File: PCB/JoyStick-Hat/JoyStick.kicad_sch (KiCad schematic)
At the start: 18 parts, among them J10 Conn_01x02_Pin, J11 Conn_01x02_Pin, J12 Conn_01x02_Pin, J13 Conn_01x02_Pin, J14 Conn_01x03_Pin, J15 Conn_01x03_Pin, J8 Conn_01x04_Pin, J9 Conn_01x04_Pin

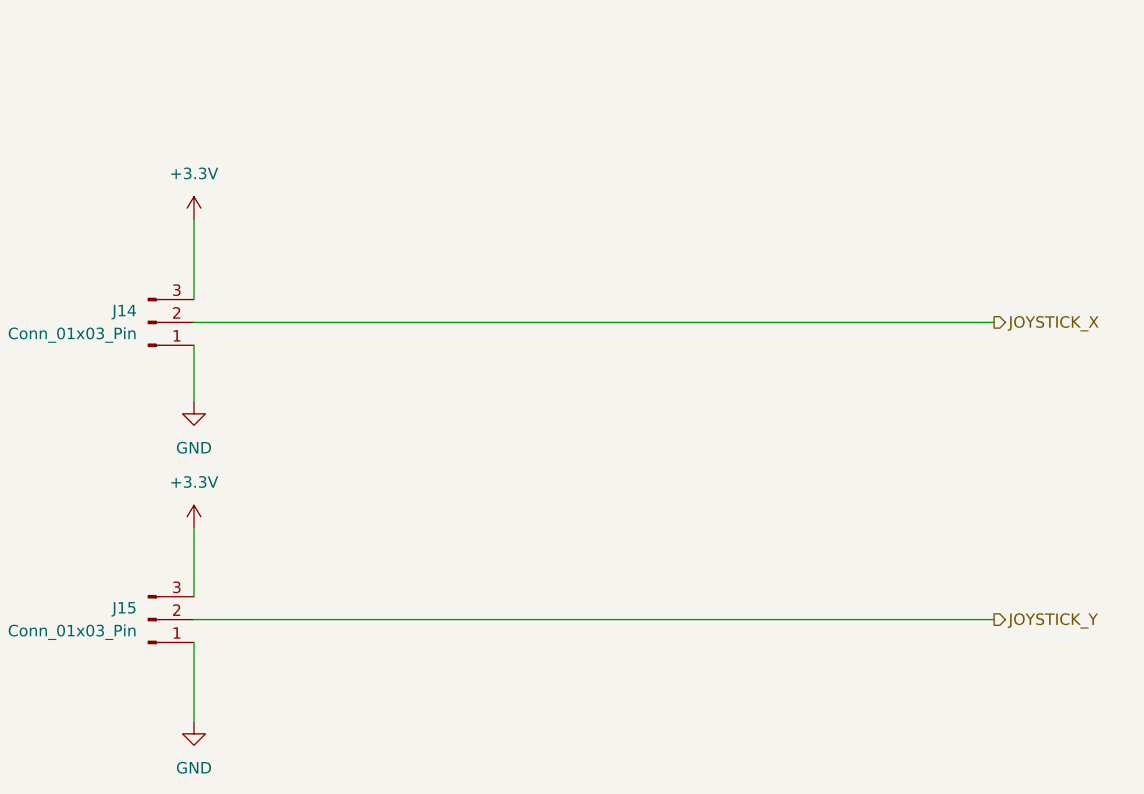
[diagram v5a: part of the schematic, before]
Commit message: Board Shape and Layout
Board Shape added and layout started !
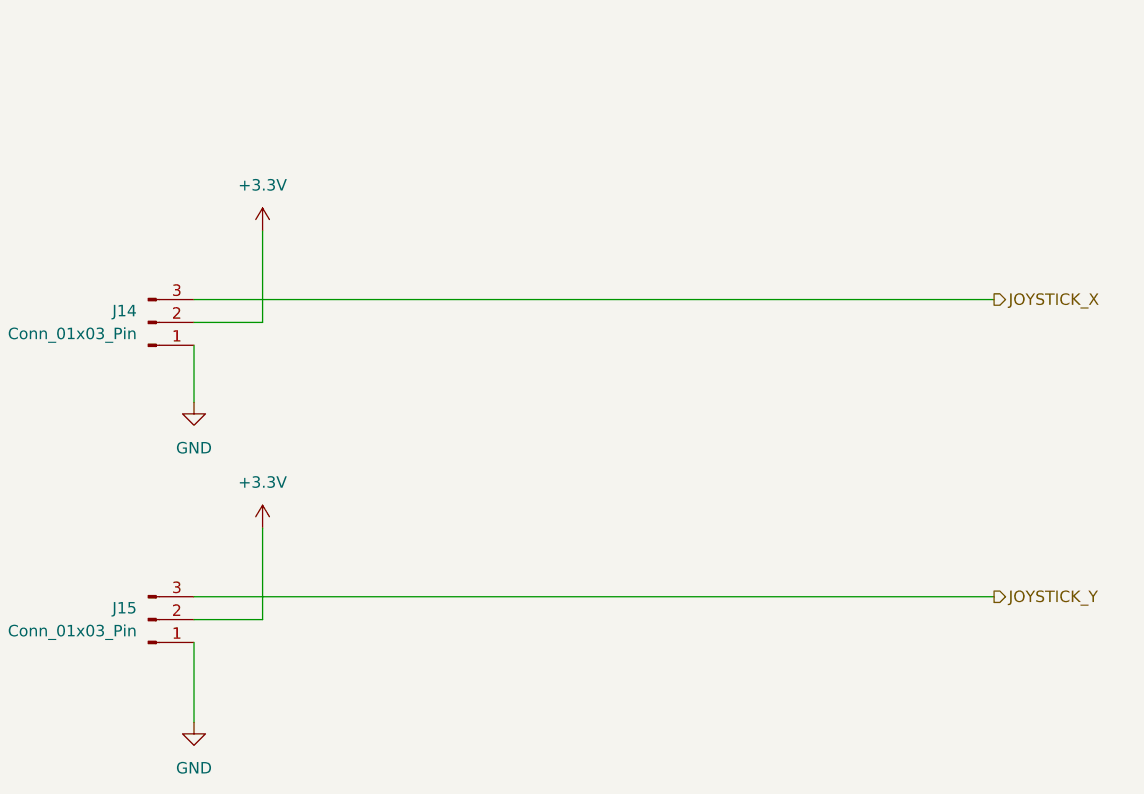
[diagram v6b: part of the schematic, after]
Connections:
- net +3.3V: now also J14.2 (Pin_2), J15.2 (Pin_2); no longer J14.3 (Pin_3), J15.3 (Pin_3)
- net JOYSTICK_X: now also J14.3 (Pin_3); no longer J14.2 (Pin_2)
- net JOYSTICK_Y: now also J15.3 (Pin_3); no longer J15.2 (Pin_2)
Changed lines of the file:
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@@
+    (stroke (width 0) (type default))
+  )
+  (wire (pts (xy 182.88 71.12) (xy 271.78 71.12))
     (stroke (width 0) (type default))
   )
@@
     (stroke (width 0) (type default))
   )
-  (wire (pts (xy 271.78 106.68) (xy 182.88 106.68))
-    (stroke (width 0) (type default))
-  )
   (wire (pts (xy 82.55 76.2) (xy 109.22 76.2))
     (stroke (width 0) (type default))
@@
     (stroke (width 0) (type default))
   )
+  (wire (pts (xy 182.88 104.14) (xy 271.78 104.14))
+    (stroke (width 0) (type default))
+  )
+  (wire (pts (xy 190.5 73.66) (xy 182.88 73.66))
+    (stroke (width 0) (type default))
+  )
   (wire (pts (xy 109.22 114.3) (xy 90.17 114.3))
     (stroke (width 0) (type default))
@@
     (stroke (width 0) (type default))
   )
+  (wire (pts (xy 190.5 96.52) (xy 190.5 106.68))
+    (stroke (width 0) (type default))
+  )
   (wire (pts (xy 76.2 71.12) (xy 76.2 73.66))
     (stroke (width 0) (type default))
@@
     (stroke (width 0) (type default))
   )
-  (wire (pts (xy 271.78 73.66) (xy 182.88 73.66))
+  (wire (pts (xy 190.5 63.5) (xy 190.5 73.66))
+    (stroke (width 0) (type default))
+  )
+  (wire (pts (xy 190.5 106.68) (xy 182.88 106.68))
     (stroke (width 0) (type default))
   )
@@
     (stroke (width 0) (type default))
   )
-  (wire (pts (xy 182.88 62.23) (xy 182.88 71.12))
-    (stroke (width 0) (type default))
-  )
   (wire (pts (xy 30.48 92.71) (xy 57.15 92.71))
     (stroke (width 0) (type default))
@@
   )
   (wire (pts (xy 182.88 76.2) (xy 182.88 82.55))
-    (stroke (width 0) (type default))
-  )
-  (wire (pts (xy 182.88 96.52) (xy 182.88 104.14))
     (stroke (width 0) (type default))
   )
@@
     (effects (font (size 1.27 1.27)) (justify right))
   )
-  (hierarchical_label "JOYSTICK_X" (shape output) (at 271.78 73.66 0) (fields_autoplaced)
+  (hierarchical_label "JOYSTICK_X" (shape output) (at 271.78 71.12 0) (fields_autoplaced)
     (effects (font (size 1.27 1.27)) (justify left))
   )
@@
     (effects (font (size 1.27 1.27)) (justify right))
   )
-  (hierarchical_label "JOYSTICK_Y" (shape output) (at 271.78 106.68 0) (fields_autoplaced)
+  (hierarchical_label "JOYSTICK_Y" (shape output) (at 271.78 104.14 0) (fields_autoplaced)
     (effects (font (size 1.27 1.27)) (justify left))
   )
@@
     )
   )
-  (symbol (lib_id "power:+3.3V") (at 182.88 96.52 0) (mirror y) (unit 1)
+  (symbol (lib_id "power:+3.3V") (at 190.5 96.52 0) (mirror y) (unit 1)
     (in_bom yes) (on_board yes) (dnp no) (fields_autoplaced)
-    (property "Reference" "#PWR062" (at 182.88 100.33 0)
-      (effects (font (size 1.27 1.27)) hide)
-    )
-    (property "Value" "+3.3V" (at 182.88 91.44 0)
-      (effects (font (size 1.27 1.27)))
-    )
-    (property "Footprint" "" (at 182.88 96.52 0)
-      (effects (font (size 1.27 1.27)) hide)
-    )
-    (property "Datasheet" "" (at 182.88 96.52 0)
+    (property "Reference" "#PWR062" (at 190.5 100.33 0)
+      (effects (font (size 1.27 1.27)) hide)
+    )
+    (property "Value" "+3.3V" (at 190.5 91.44 0)
+      (effects (font (size 1.27 1.27)))
+    )
+    (property "Footprint" "" (at 190.5 96.52 0)
+      (effects (font (size 1.27 1.27)) hide)
+    )
+    (property "Datasheet" "" (at 190.5 96.52 0)
       (effects (font (size 1.27 1.27)) hide)
     )
@@
     )
   )
-  (symbol (lib_id "power:+3.3V") (at 182.88 62.23 0) (mirror y) (unit 1)
+  (symbol (lib_id "power:+3.3V") (at 190.5 63.5 0) (mirror y) (unit 1)
     (in_bom yes) (on_board yes) (dnp no) (fields_autoplaced)
-    (property "Reference" "#PWR060" (at 182.88 66.04 0)
-      (effects (font (size 1.27 1.27)) hide)
-    )
-    (property "Value" "+3.3V" (at 182.88 57.15 0)
-      (effects (font (size 1.27 1.27)))
-    )
-    (property "Footprint" "" (at 182.88 62.23 0)
-      (effects (font (size 1.27 1.27)) hide)
-    )
-    (property "Datasheet" "" (at 182.88 62.23 0)
-      (effects (font (size 1.27 1.27)) hide)
-    )
+    (property "Reference" "#PWR060" (at 190.5 67.31 0)
+      (effects (font (size 1.27 1.27)) hide)
+    )
+    (property "Value" "+3.3V" (at 190.5 58.42 0)
+      (effects (font (size 1.27 1.27)))
+    )
+    (property "Footprint" "" (at 190.5 63.5 0)
+      (effects (font (size 1.27 1.27)) hide)
+    )
+    (property "Datasheet" "" (at 190.5 63.5 0)
+      (effects (font (size 1.27 1.27)) hide)
+    )

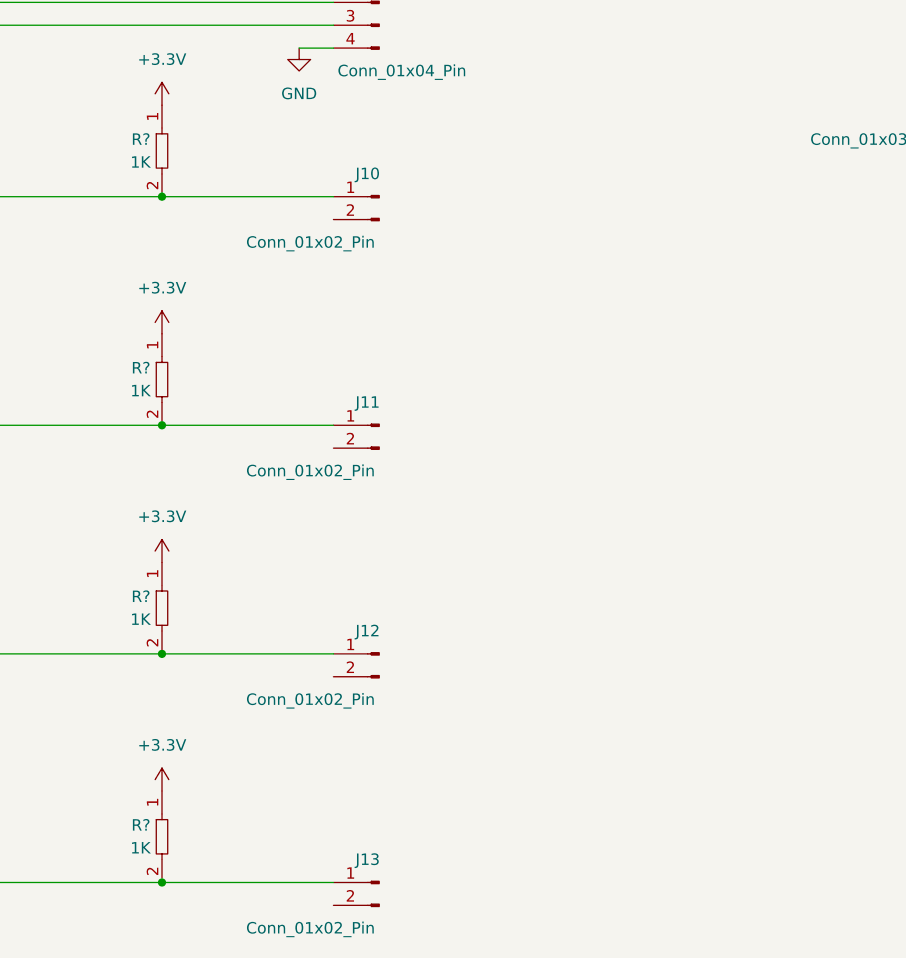
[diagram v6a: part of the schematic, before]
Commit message: Board Tweaks and progress
Made progress with baord. Adjusted the position of RPi header to be correct and absolute. Changed location of regulator modules and power input capacitors. Added 3D models missing from the larger components. Changed connectors and positions for just about everything. Added connnector for LED driver duagher board .
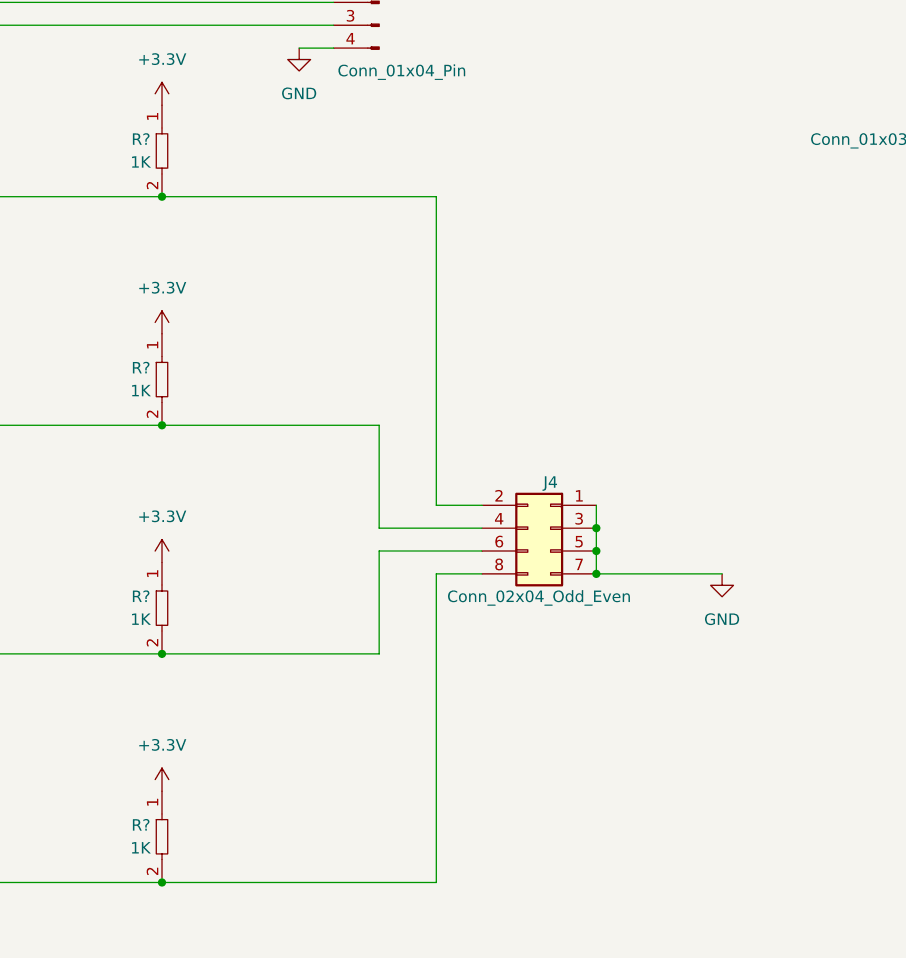
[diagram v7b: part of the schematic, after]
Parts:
- removed J10, J11, J12, J13: Conn_01x02_Pin, Connector_PinHeader_2.54mm:PinHeader_1x02_P2.54mm_Vertical, symbol Connector:Conn_01x02_Pin
- added J4: Conn_02x04_Odd_Even, Connector_PinHeader_2.54mm:PinHeader_2x04_P2.54mm_Vertical, symbol Connector_Generic:Conn_02x04_Odd_Even
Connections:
- net BUTTON1: now also J4.2 (Pin_2)
- net BUTTON2: now also J4.4 (Pin_4)
- net BUTTON3: now also J4.6 (Pin_6)
- net BUTTON4: now also J4.8 (Pin_8)
- net GND: now also J4.1 (Pin_1), J4.3 (Pin_3), J4.5 (Pin_5), J4.7 (Pin_7)
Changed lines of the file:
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@@
   (junction (at 90.17 165.1) (diameter 0) (color 0 0 0 0)
   )
+  (junction (at 138.43 151.13) (diameter 0) (color 0 0 0 0)
+  )
   (junction (at 90.17 190.5) (diameter 0) (color 0 0 0 0)
   )
   (junction (at 88.9 78.74) (diameter 0) (color 0 0 0 0)
   )
+  (junction (at 138.43 153.67) (diameter 0) (color 0 0 0 0)
+  )
   (junction (at 57.15 92.71) (diameter 0) (color 0 0 0 0)
   )
@@
   (junction (at 50.8 90.17) (diameter 0) (color 0 0 0 0)
   )
+  (junction (at 138.43 156.21) (diameter 0) (color 0 0 0 0)
+  )
   (junction (at 90.17 139.7) (diameter 0) (color 0 0 0 0)
   )
+  (wire (pts (xy 120.65 148.59) (xy 125.73 148.59))
+    (stroke (width 0) (type default))
+  )
   (wire (pts (xy 63.5 95.25) (xy 109.22 95.25))
     (stroke (width 0) (type default))
   )
+  (wire (pts (xy 120.65 156.21) (xy 125.73 156.21))
+    (stroke (width 0) (type default))
+  )
+  (wire (pts (xy 138.43 148.59) (xy 138.43 151.13))
+    (stroke (width 0) (type default))
+  )
   (wire (pts (xy 88.9 71.12) (xy 88.9 78.74))
     (stroke (width 0) (type default))
   )
+  (wire (pts (xy 114.3 153.67) (xy 125.73 153.67))
+    (stroke (width 0) (type default))
+  )
   (wire (pts (xy 182.88 71.12) (xy 271.78 71.12))
     (stroke (width 0) (type default))
@@
     (stroke (width 0) (type default))
   )
-  (wire (pts (xy 109.22 139.7) (xy 90.17 139.7))
+  (wire (pts (xy 90.17 139.7) (xy 114.3 139.7))
+    (stroke (width 0) (type default))
+  )
+  (wire (pts (xy 114.3 151.13) (xy 125.73 151.13))
     (stroke (width 0) (type default))
   )
@@
     (stroke (width 0) (type default))
   )
-  (wire (pts (xy 109.22 114.3) (xy 90.17 114.3))
-    (stroke (width 0) (type default))
-  )
-  (wire (pts (xy 109.22 190.5) (xy 90.17 190.5))
+  (wire (pts (xy 90.17 114.3) (xy 120.65 114.3))
+    (stroke (width 0) (type default))
+  )
+  (wire (pts (xy 90.17 190.5) (xy 120.65 190.5))
     (stroke (width 0) (type default))
   )
@@
     (stroke (width 0) (type default))
   )
+  (wire (pts (xy 138.43 156.21) (xy 152.4 156.21))
+    (stroke (width 0) (type default))
+  )
+  (wire (pts (xy 114.3 165.1) (xy 114.3 153.67))
+    (stroke (width 0) (type default))
+  )
   (wire (pts (xy 57.15 71.12) (xy 57.15 92.71))
     (stroke (width 0) (type default))
@@
     (stroke (width 0) (type default))
   )
+  (wire (pts (xy 120.65 190.5) (xy 120.65 156.21))
+    (stroke (width 0) (type default))
+  )
   (wire (pts (xy 30.48 92.71) (xy 57.15 92.71))
     (stroke (width 0) (type default))
@@
     (stroke (width 0) (type default))
   )
+  (wire (pts (xy 138.43 153.67) (xy 138.43 156.21))
+    (stroke (width 0) (type default))
+  )
   (wire (pts (xy 88.9 78.74) (xy 109.22 78.74))
     (stroke (width 0) (type default))
   )
+  (wire (pts (xy 120.65 114.3) (xy 120.65 148.59))
+    (stroke (width 0) (type default))
+  )
   (wire (pts (xy 30.48 95.25) (xy 63.5 95.25))
     (stroke (width 0) (type default))
@@
     (stroke (width 0) (type default))
   )
+  (wire (pts (xy 138.43 151.13) (xy 138.43 153.67))
+    (stroke (width 0) (type default))
+  )
   (wire (pts (xy 90.17 139.7) (xy 24.13 139.7))
     (stroke (width 0) (type default))
   )
-  (wire (pts (xy 109.22 165.1) (xy 90.17 165.1))
+  (wire (pts (xy 90.17 165.1) (xy 114.3 165.1))
     (stroke (width 0) (type default))
   )
   (wire (pts (xy 50.8 90.17) (xy 109.22 90.17))
+    (stroke (width 0) (type default))
+  )
+  (wire (pts (xy 114.3 139.7) (xy 114.3 151.13))
     (stroke (width 0) (type default))
   )
@@
     (effects (font (size 1.27 1.27)) (justify right))
   )
-  (symbol (lib_id "Connector:Conn_01x02_Pin") (at 114.3 114.3 0) (mirror y) (unit 1)
-    (in_bom yes) (on_board yes) (dnp no)
-    (property "Reference" "J10" (at 113.03 111.76 0)
-      (effects (font (size 1.27 1.27)))
-    )
-    (property "Value" "Conn_01x02_Pin" (at 106.68 119.38 0)
-      (effects (font (size 1.27 1.27)))
-    )
-    (property "Footprint" "Connector_PinHeader_2.54mm:PinHeader_1x02_P2.54mm_Vertical" (at 114.3 114.3 0)
-      (effects (font (size 1.27 1.27)) hide)
-    )
-    (property "Datasheet" "~" (at 114.3 114.3 0)
-      (effects (font (size 1.27 1.27)) hide)
-    )
-    (pin "1")
-    (pin "2")
-    (instances
-      (project "JoyStick-Hat"
-        (path "/cf0c81b5-5bdf-47c3-83c0-f6980f515e65/657fac1d-f0e2-4536-8020-58a2ff4b82f6"
-          (reference "J10") (unit 1)
-        )
-      )
-    )
-  )
-  (symbol (lib_id "Connector:Conn_01x02_Pin") (at 114.3 139.7 0) (mirror y) (unit 1)
-    (in_bom yes) (on_board yes) (dnp no)
-    (property "Reference" "J11" (at 113.03 137.16 0)
-      (effects (font (size 1.27 1.27)))
-    )
-    (property "Value" "Conn_01x02_Pin" (at 106.68 144.78 0)
-      (effects (font (size 1.27 1.27)))
-    )
-    (property "Footprint" "Connector_PinHeader_2.54mm:PinHeader_1x02_P2.54mm_Vertical" (at 114.3 139.7 0)
-      (effects (font (size 1.27 1.27)) hide)
-    )
-    (property "Datasheet" "~" (at 114.3 139.7 0)
-      (effects (font (size 1.27 1.27)) hide)
-    )
-    (pin "1")
-    (pin "2")
-    (instances
-      (project "JoyStick-Hat"
-        (path "/cf0c81b5-5bdf-47c3-83c0-f6980f515e65/657fac1d-f0e2-4536-8020-58a2ff4b82f6"
-          (reference "J11") (unit 1)
-        )
-      )
-    )
-  )
   (symbol (lib_id "Connector:Conn_01x03_Pin") (at 177.8 73.66 0) (mirror x) (unit 1)
     (in_bom yes) (on_board yes) (dnp no) (fields_autoplaced)
@@
         (path "/cf0c81b5-5bdf-47c3-83c0-f6980f515e65/657fac1d-f0e2-4536-8020-58a2ff4b82f6"
           (reference "#PWR063") (unit 1)
+        )
+      )
+    )
+  )
+  (symbol (lib_id "power:GND") (at 152.4 156.21 0) (mirror y) (unit 1)
+    (in_bom yes) (on_board yes) (dnp no) (fields_autoplaced)
+    (property "Reference" "#PWR021" (at 152.4 162.56 0)
+      (effects (font (size 1.27 1.27)) hide)
+    )
+    (property "Value" "GND" (at 152.4 161.29 0)
+      (effects (font (size 1.27 1.27)))
+    )
+    (property "Footprint" "" (at 152.4 156.21 0)
+      (effects (font (size 1.27 1.27)) hide)
+    )
+    (property "Datasheet" "" (at 152.4 156.21 0)
+      (effects (font (size 1.27 1.27)) hide)
+    )
+    (pin "1")
+    (instances
+      (project "JoyStick-Hat"
+        (path "/cf0c81b5-5bdf-47c3-83c0-f6980f515e65/657fac1d-f0e2-4536-8020-58a2ff4b82f6"
+          (reference "#PWR021") (unit 1)
         )
       )
@@
     )
   )
-  (symbol (lib_id "Connector:Conn_01x02_Pin") (at 114.3 165.1 0) (mirror y) (unit 1)
-    (in_bom yes) (on_board yes) (dnp no)
-    (property "Reference" "J12" (at 113.03 162.56 0)
-      (effects (font (size 1.27 1.27)))
-    )
-    (property "Value" "Conn_01x02_Pin" (at 106.68 170.18 0)
-      (effects (font (size 1.27 1.27)))
-    )
-    (property "Footprint" "Connector_PinHeader_2.54mm:PinHeader_1x02_P2.54mm_Vertical" (at 114.3 165.1 0)
-      (effects (font (size 1.27 1.27)) hide)
-    )
-    (property "Datasheet" "~" (at 114.3 165.1 0)
-      (effects (font (size 1.27 1.27)) hide)
-    )
-    (pin "1")
-    (pin "2")
-    (instances
-      (project "JoyStick-Hat"
-        (path "/cf0c81b5-5bdf-47c3-83c0-f6980f515e65/657fac1d-f0e2-4536-8020-58a2ff4b82f6"
-          (reference "J12") (unit 1)
-        )
-      )
-    )
-  )
   (symbol (lib_id "power:GND") (at 105.41 97.79 0) (mirror y) (unit 1)
     (in_bom yes) (on_board yes) (dnp no) (fields_autoplaced)
@@
     )
   )
-  (symbol (lib_id "Connector:Conn_01x02_Pin") (at 114.3 190.5 0) (mirror y) (unit 1)
+  (symbol (lib_id "Connector_Generic:Conn_02x04_Odd_Even") (at 133.35 151.13 0) (mirror y) (unit 1)
     (in_bom yes) (on_board yes) (dnp no)
-    (property "Reference" "J13" (at 113.03 187.96 0)
-      (effects (font (size 1.27 1.27)))
-    )
-    (property "Value" "Conn_01x02_Pin" (at 106.68 195.58 0)
-      (effects (font (size 1.27 1.27)))
-    )
-    (property "Footprint" "Connector_PinHeader_2.54mm:PinHeader_1x02_P2.54mm_Vertical" (at 114.3 190.5 0)
-      (effects (font (size 1.27 1.27)) hide)
-    )
-    (property "Datasheet" "~" (at 114.3 190.5 0)
-      (effects (font (size 1.27 1.27)) hide)
-    )
-    (pin "1")
+    (property "Reference" "J4" (at 133.35 146.05 0)
+      (effects (font (size 1.27 1.27)))
+    )
+    (property "Value" "Conn_02x04_Odd_Even" (at 132.08 158.75 0)
+      (effects (font (size 1.27 1.27)))
+    )
+    (property "Footprint" "Connector_PinHeader_2.54mm:PinHeader_2x04_P2.54mm_Vertical" (at 133.35 151.13 0)
+      (effects (font (size 1.27 1.27)) hide)
+    )
+    (property "Datasheet" "~" (at 133.35 151.13 0)
+      (effects (font (size 1.27 1.27)) hide)
+    )
     (pin "2")
-    (instances
-      (project "JoyStick-Hat"
-        (path "/cf0c81b5-5bdf-47c3-83c0-f6980f515e65/657fac1d-f0e2-4536-8020-58a2ff4b82f6"
-          (reference "J13") (unit 1)
-        )
-      )
+    (pin "4")
+    (pin "3")
+    (pin "5")
+    (pin "6")
+    (pin "1")
+    (pin "7")
+    (pin "8")
+    (instances
+      (project "JoyStick-Hat"
+        (path "/cf0c81b5-5bdf-47c3-83c0-f6980f515e65/657fac1d-f0e2-4536-8020-58a2ff4b82f6"
+          (reference "J4") (unit 1)
+        )
+      )
